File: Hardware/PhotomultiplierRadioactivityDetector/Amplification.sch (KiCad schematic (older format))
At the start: 35 parts, among them U1 TL074, U2 TL074

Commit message: add missing footprints
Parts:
- C43: footprint Capacitors_Tantalum_SMD:CP_Tantalum_Case-A_EIA-3216-18_Hand -> Capacitor_Tantalum_SMD:CP_EIA-3528-21_Kemet-B
- L1: footprint Inductors_SMD:L_1812 -> Inductor_SMD:L_0805_2012Metric
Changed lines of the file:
@@
 F 0 "L1" V 10000 3650 50  0000 C CNN
 F 1 "u68" V 10150 3750 50  0000 C CNN
-F 2 "Inductors_SMD:L_1812" H 10050 3650 50  0001 C CNN
+F 2 "Inductor_SMD:L_0805_2012Metric" H 10050 3650 50  0001 C CNN
 F 3 "" H 10050 3650 50  0001 C CNN
 	1    10050 3650
@@
 F 0 "C43" V 9950 4200 50  0000 L CNN
 F 1 "1u/16V" V 9850 4200 50  0000 L CNN
-F 2 "Capacitors_Tantalum_SMD:CP_Tantalum_Case-A_EIA-3216-18_Hand" H 9838 3950 50  0001 C CNN
+F 2 "Capacitor_Tantalum_SMD:CP_EIA-3528-21_Kemet-B" H 9838 3950 50  0001 C CNN
 F 3 "" H 9800 4100 50  0001 C CNN
 	1    9800 4100

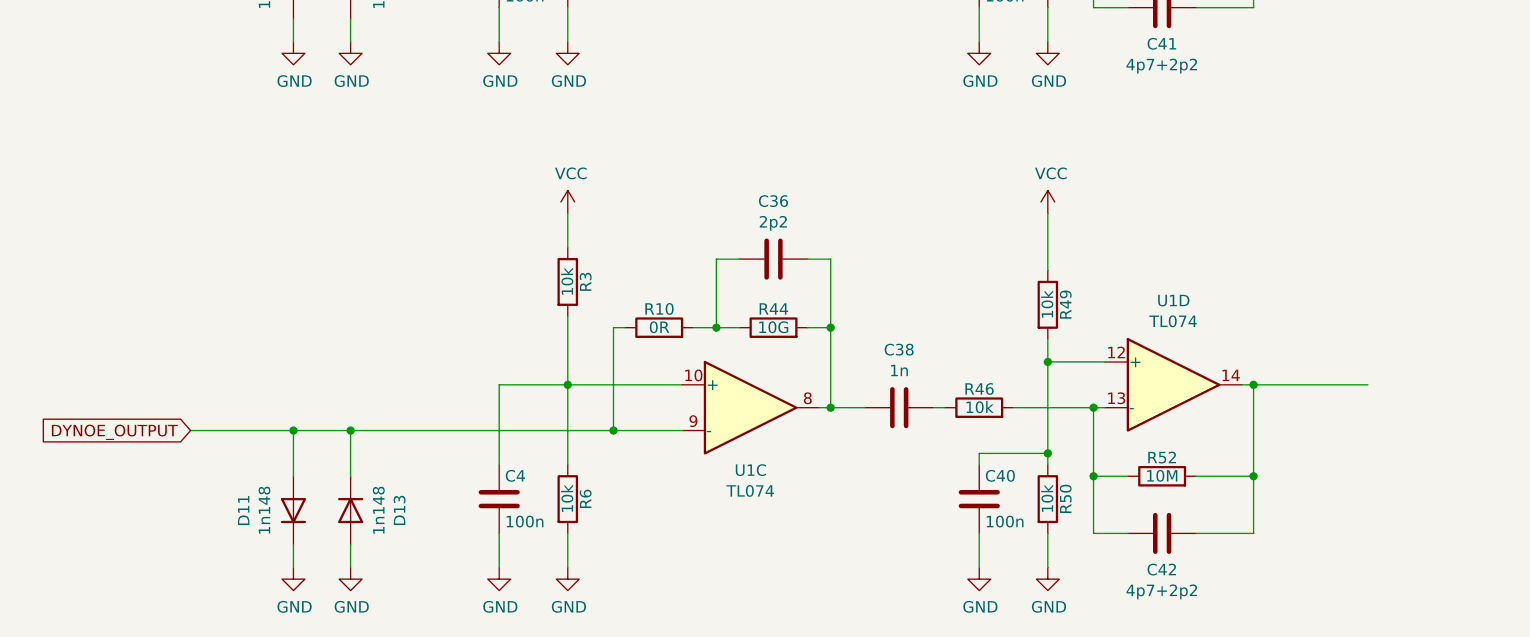
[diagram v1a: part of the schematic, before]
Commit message: reworked power supply for tube
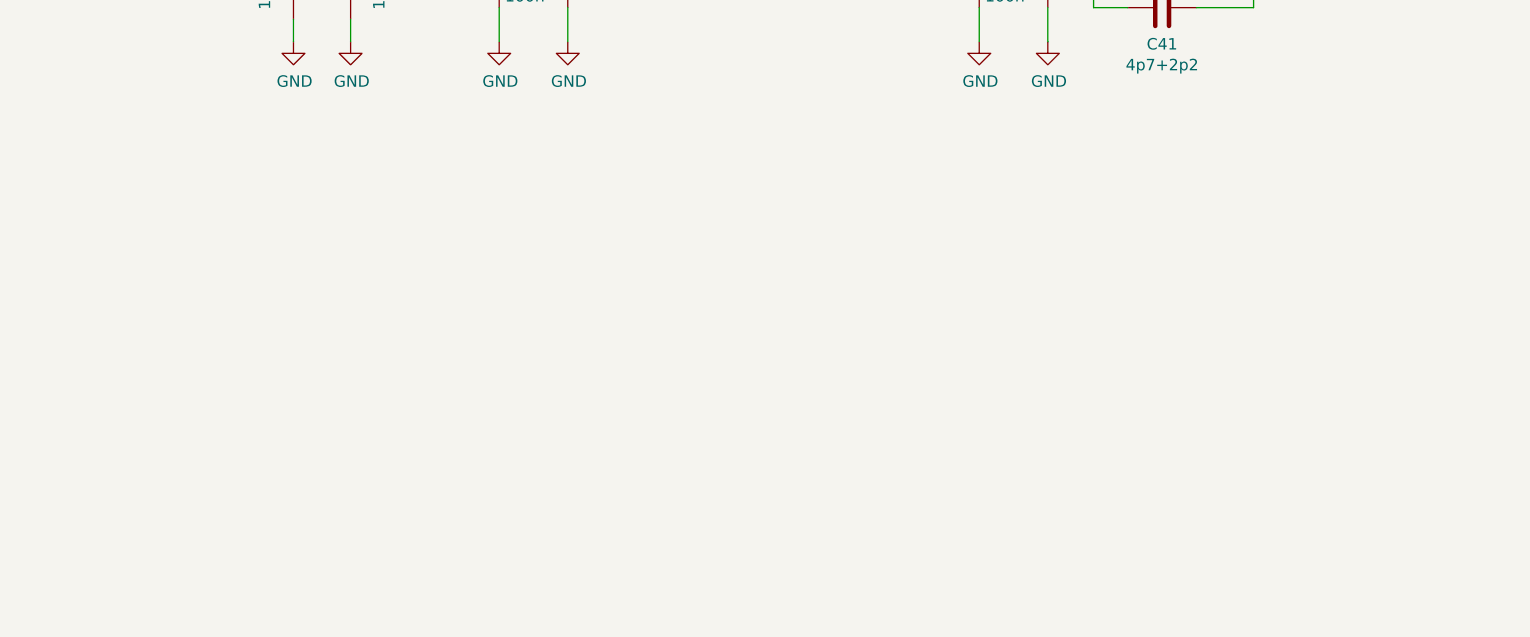
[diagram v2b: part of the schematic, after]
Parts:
- removed C36: 2p2, Capacitor_SMD:C_0805_2012Metric_Pad1.15x1.40mm_HandSolder, symbol Device:C
- removed C38: 1n, Capacitor_SMD:C_0805_2012Metric_Pad1.15x1.40mm_HandSolder, symbol Device:C
- removed C4, C40: 100n, Capacitor_SMD:C_0805_2012Metric_Pad1.15x1.40mm_HandSolder, symbol Device:C
- removed C42: 4p7+2p2, Capacitor_SMD:C_0805_2012Metric_Pad1.15x1.40mm_HandSolder, symbol Device:C
- removed D11, D13: 1n148, Diode_SMD:D_MELF, symbol Device:D
- removed R10: 0R, Resistor_SMD:R_0805_2012Metric_Pad1.15x1.40mm_HandSolder, symbol Device:R
- removed R3, R46, R49, R50, R6: 10k, Resistor_SMD:R_0805_2012Metric_Pad1.15x1.40mm_HandSolder, symbol Device:R
- removed R44: 10G, Resistor_SMD:R_0805_2012Metric_Pad1.15x1.40mm_HandSolder, symbol Device:R
- removed R52: 10M, Resistor_SMD:R_0805_2012Metric_Pad1.15x1.40mm_HandSolder, symbol Device:R
- removed unit 3 of U1
- removed unit 4 of U1
